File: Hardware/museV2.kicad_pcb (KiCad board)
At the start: 2 copper layers, 129 x 55.9 mm, 467 parts, among them P1 RCA_conn_x2, P10 -15V, P11 ~4, P18 RX7, P19 3.3V, P20 TX6, P21 1.8V, P22 PSU_CTL, P23 GND, P3 3.5mm_conn_tip_switch, P31 P1, P32 L1.8_1, P33 L3.3_1, P34 P2, P35 L1.8_2, P36 L3.3_2, P37 P3, P38 L1.8_3, P39 L3.3_3, P4 3.5mm_conn_tip_switch, P40 P4, P41 L1.8_4, P42 L3.3_4, P43 +5V, P5 CONN_01X06, P6 CONN_02X14, P7 ~2, P8 +15V, P9 ~3, Q1 PMOS, Q2 BSS138, SW1 PWR_BTN, SW2 PAIR_BTN, U1 TPS65130, U10 PCM1863, U11 PCM1796, U12 NE5534, U13 NE5534, U14 NE5534, U15 NE5534, U16 NE5534, U17 NE5534, U18 EdisonConnector, U19 GTL2010, U2 LP38692, U20 GTL2010, U21 GTL2010, U22 PCA9685BS, U3 PLR135/T10, U4 POM-3535L-3-R, U5 POM-3535L-3-R, U6 PLT133/T10W, U7 POM-3535L-3-R, U8 POM-3535L-3-R, U9 PCM9211, X1 24.576 MHz

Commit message: Updated text
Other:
- board text added: "Lead Hardware Designer: Jason Merlo Lead Software Designer: Steven Ploog"
- board text added: "muse v2.0.0"
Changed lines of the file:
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@@
     (links 893)
     (no_connects 152)
-    (area 103.324999 91.525 235.575001 156.088095)
+    (area 106.424999 95.424999 235.575001 151.475001)
     (thickness 1.6)
-    (drawings 4)
+    (drawings 6)
     (tracks 3081)
     (zones 0)
@@
   (page A4)
   (layers
-    (0 F.Cu signal)
-    (31 B.Cu signal)
+    (0 F.Cu signal hide)
+    (31 B.Cu signal hide)
     (32 B.Adhes user)
-    (33 F.Adhes user)
+    (33 F.Adhes user hide)
     (34 B.Paste user)
-    (35 F.Paste user)
+    (35 F.Paste user hide)
     (36 B.SilkS user)
-    (37 F.SilkS user)
+    (37 F.SilkS user hide)
     (38 B.Mask user)
-    (39 F.Mask user)
+    (39 F.Mask user hide)
     (40 Dwgs.User user)
     (41 Cmts.User user)
@@
     (45 Margin user)
     (46 B.CrtYd user)
-    (47 F.CrtYd user)
+    (47 F.CrtYd user hide)
     (48 B.Fab user hide)
     (49 F.Fab user hide)
@@
     (pad_to_mask_clearance 0.2)
     (aux_axis_origin 0 0)
-    (visible_elements FFFFFF7F)
+    (visible_elements FFFFBD7F)
     (pcbplotparams
       (layerselection 0x00030_80000001)
@@
   (module muse-v2-lib:Intel_Edison (layer F.Cu)
     (at 209.35 118.96 180)
-    (fp_text reference U18 (at 1.4 -29.1 360) (layer F.SilkS)
+    (fp_text reference U18 (at 1.4 -29.1 180) (layer F.SilkS) hide
       (effects (font (size 1 1) (thickness 0.15)))
     )
@@
     (tags "DO-214AB diode")
     (attr smd)
-    (fp_text reference D1 (at -4.117826 1.966368 180) (layer F.SilkS)
+    (fp_text reference D1 (at -4.117826 1.966368) (layer F.SilkS) hide
       (effects (font (size 1 1) (thickness 0.15)))
     )
@@
     (tags "DO-214AB diode")
     (attr smd)
-    (fp_text reference D2 (at -3.584 1.8 180) (layer F.SilkS)
+    (fp_text reference D2 (at -3.584 1.8 180) (layer F.SilkS) hide
       (effects (font (size 1 1) (thickness 0.15)))
     )
@@
   (module muse-v2-lib:7.3mm-Inductor (layer F.Cu)
     (at 162.717826 118.45 180)
-    (fp_text reference L1 (at 5 0 270) (layer F.SilkS)
+    (fp_text reference L1 (at 5 0 270) (layer F.SilkS) hide
       (effects (font (size 1 1) (thickness 0.15)))
     )
@@
   (module muse-v2-lib:7.3mm-Inductor (layer F.Cu)
     (at 176.717826 102.783632 90)
-    (fp_text reference L2 (at 4.8 0 180) (layer F.SilkS)
+    (fp_text reference L2 (at 4.8 0 180) (layer F.SilkS) hide
       (effects (font (size 1 1) (thickness 0.15)))
     )
@@
     (descr "Through hole pin header")
     (tags "pin header")
-    (fp_text reference P6 (at -2.35 -0.01 360) (layer F.SilkS)
+    (fp_text reference P6 (at -2.35 -0.01 360) (layer F.SilkS) hide
       (effects (font (size 1 1) (thickness 0.15)))
     )
@@
     (tags "resistor 0402")
     (attr smd)
-    (fp_text reference R45 (at 0 1.8 180) (layer B.SilkS)
+    (fp_text reference R45 (at 0 1.8 180) (layer B.SilkS) hide
       (effects (font (size 1 1) (thickness 0.15)) (justify mirror))
     )
@@
     (tags "resistor 0402")
     (attr smd)
-    (fp_text reference R47 (at 0 1.8 270) (layer B.SilkS)
+    (fp_text reference R47 (at 0 1.8 270) (layer B.SilkS) hide
       (effects (font (size 1 1) (thickness 0.15)) (justify mirror))
     )
@@
     (tags "resistor 0402")
     (attr smd)
-    (fp_text reference R49 (at 0 1.8 270) (layer B.SilkS)
+    (fp_text reference R49 (at 0 1.8 360) (layer B.SilkS) hide
       (effects (font (size 1 1) (thickness 0.15)) (justify mirror))
     )
@@
     (tags "resistor 0402")
     (attr smd)
-    (fp_text reference R51 (at 0 1.8 180) (layer B.SilkS)
+    (fp_text reference R51 (at 0 1.8 180) (layer B.SilkS) hide
       (effects (font (size 1 1) (thickness 0.15)) (justify mirror))
     )
@@
     (tags "resistor 0402")
     (attr smd)
-    (fp_text reference R53 (at 0 1.8 180) (layer B.SilkS)
+    (fp_text reference R53 (at 0 1.8 180) (layer B.SilkS) hide
       (effects (font (size 1 1) (thickness 0.15)) (justify mirror))
     )
@@
     (tags "resistor 0402")
     (attr smd)
-    (fp_text reference R54 (at 0 1.8 180) (layer B.SilkS)
+    (fp_text reference R54 (at 0 1.8 180) (layer B.SilkS) hide
       (effects (font (size 1 1) (thickness 0.15)) (justify mirror))
     )
@@
     (tags "SSOP 0.65")
     (attr smd)
-    (fp_text reference U19 (at 0 -5.25 180) (layer F.SilkS)
+    (fp_text reference U19 (at 0 -5.25 180) (layer F.SilkS) hide
       (effects (font (size 1 1) (thickness 0.15)))
     )
@@
     (tags "SSOP 0.65")
     (attr smd)
-    (fp_text reference U20 (at 0 -5.25) (layer F.SilkS)
+    (fp_text reference U20 (at 0 -5.25) (layer F.SilkS) hide
       (effects (font (size 1 1) (thickness 0.15)))
     )
@@
     (tags "SSOP 0.65")
     (attr smd)
-    (fp_text reference U21 (at 0 -5.25) (layer F.SilkS)
+    (fp_text reference U21 (at 0 -5.25) (layer F.SilkS) hide
       (effects (font (size 1 1) (thickness 0.15)))
     )
@@
     (tags "QFP 0.5")
     (attr smd)
-    (fp_text reference U9 (at -4.25 -4.45) (layer F.SilkS)
+    (fp_text reference U9 (at -4.25 -4.45) (layer F.SilkS) hide
       (effects (font (size 1 1) (thickness 0.15)))
     )
@@
   (module muse-v2-lib:5x3.2mm_crystal (layer F.Cu)
     (at 180.15 118.25 315)
-    (fp_text reference X1 (at -0.883883 -3.075914 315) (layer F.SilkS)
+    (fp_text reference X1 (at -0.883883 -3.075914 315) (layer F.SilkS) hide
       (effects (font (size 1 1) (thickness 0.15)))
     )
@@
     (tags "QFN 0.65")
     (attr smd)
-    (fp_text reference U22 (at -3.068321 -3.869561 315) (layer F.SilkS)
+    (fp_text reference U22 (at -3.068321 -3.869561 315) (layer F.SilkS) hide
       (effects (font (size 1 1) (thickness 0.15)))
     )
@@
     (descr "SMT capacitor, aluminium electrolytic, 4x5.3")
     (attr smd)
-    (fp_text reference C15 (at 0 -3.5433 90) (layer B.SilkS)
+    (fp_text reference C15 (at 0 -3.5433 90) (layer B.SilkS) hide
       (effects (font (size 1 1) (thickness 0.15)) (justify mirror))
     )
@@
     (descr "SMT capacitor, aluminium electrolytic, 4x5.3")
     (attr smd)
-    (fp_text reference C17 (at 0 -3.5433 180) (layer B.SilkS)
+    (fp_text reference C17 (at 0 -3.5433 180) (layer B.SilkS) hide
       (effects (font (size 1 1) (thickness 0.15)) (justify mirror))
     )
@@
     (descr "SMT capacitor, aluminium electrolytic, 4x5.3")
     (attr smd)
-    (fp_text reference C22 (at 0 -3.5433) (layer B.SilkS)
+    (fp_text reference C22 (at 0 -3.5433) (layer B.SilkS) hide
       (effects (font (size 1 1) (thickness 0.15)) (justify mirror))
     )
@@
     (descr "SMT capacitor, aluminium electrolytic, 4x5.3")
     (attr smd)
-    (fp_text reference C24 (at 0 3.5433) (layer F.SilkS)
+    (fp_text reference C24 (at 0 3.5433) (layer F.SilkS) hide
       (effects (font (size 1 1) (thickness 0.15)))
     )
@@
     (descr "SMT capacitor, aluminium electrolytic, 4x5.3")
     (attr smd)
-    (fp_text reference C38 (at 0 -3.5433 135) (layer B.SilkS)
+    (fp_text reference C38 (at 0 -3.5433 135) (layer B.SilkS) hide
       (effects (font (size 1 1) (thickness 0.15)) (justify mirror))
     )
@@
     (descr "SMT capacitor, aluminium electrolytic, 4x5.3")
     (attr smd)
-    (fp_text reference C82 (at 0 -3.5433 90) (layer B.SilkS)
+    (fp_text reference C82 (at 0 -3.5433 90) (layer B.SilkS) hide
       (effects (font (size 1 1) (thickness 0.15)) (justify mirror))
     )
@@
     (descr "SMT capacitor, aluminium electrolytic, 4x5.3")
     (attr smd)
-    (fp_text reference C87 (at 0 -3.5433 90) (layer B.SilkS)
+    (fp_text reference C87 (at 0 -3.5433 90) (layer B.SilkS) hide
       (effects (font (size 1 1) (thickness 0.15)) (justify mirror))
     )
@@
     (descr "SMT capacitor, aluminium electrolytic, 4x5.3")
     (attr smd)
-    (fp_text reference C91 (at 0 -3.5433 90) (layer B.SilkS)
+    (fp_text reference C91 (at 0 -3.5433 90) (layer B.SilkS) hide
       (effects (font (size 1 1) (thickness 0.15)) (justify mirror))
     )
@@
     )
   )
+  (gr_text "Lead Hardware Designer: Jason Merlo\nLead Software Designer: Steven Ploog" (at 233.25 105.15) (layer B.SilkS)
+    (effects (font (size 0.75 0.75) (thickness 0.125)) (justify left mirror))
+  )
+  (gr_text "muse v2.0.0\n" (at 233.45 102.35) (layer B.SilkS)
+    (effects (font (size 2 2) (thickness 0.3)) (justify left mirror))
+  )
   (gr_line (start 106.5 151.4) (end 235.5 151.4) (layer Edge.Cuts) (width 0.15))

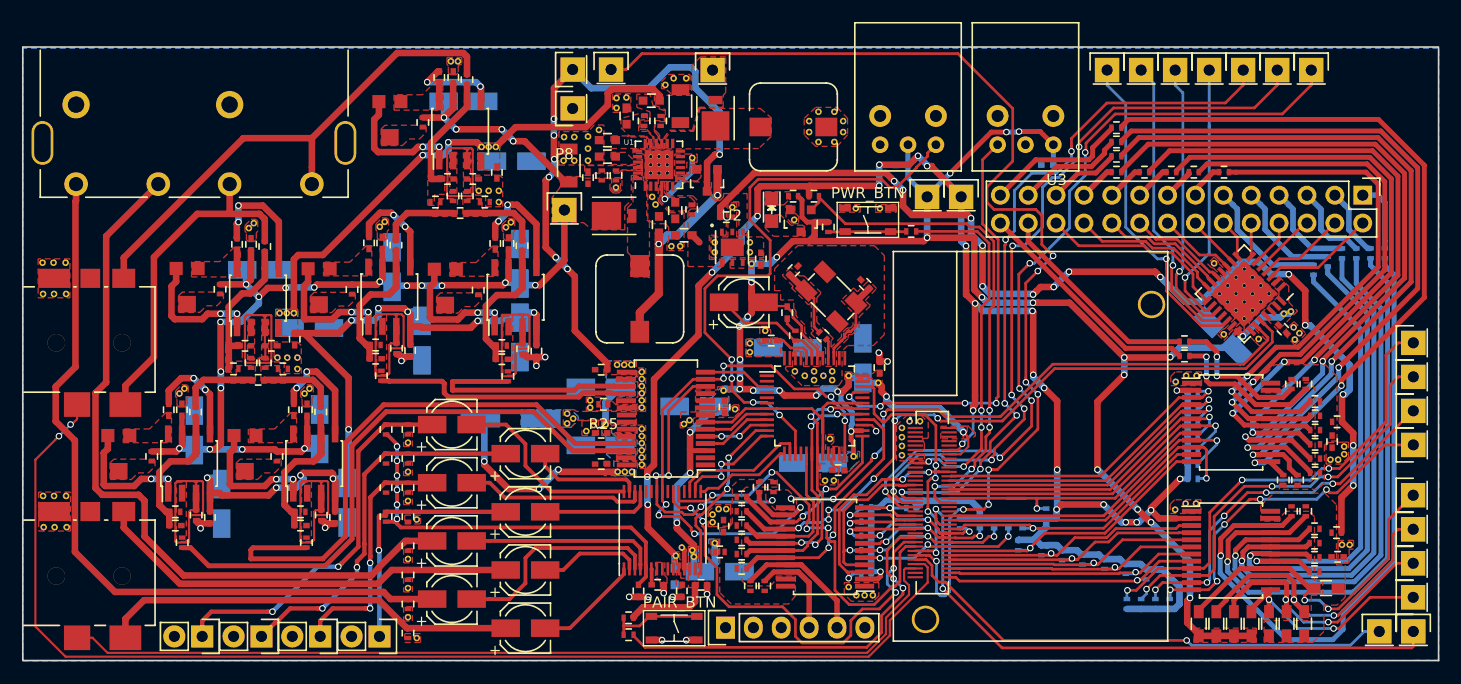
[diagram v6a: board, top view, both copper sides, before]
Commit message: Mounting holes added
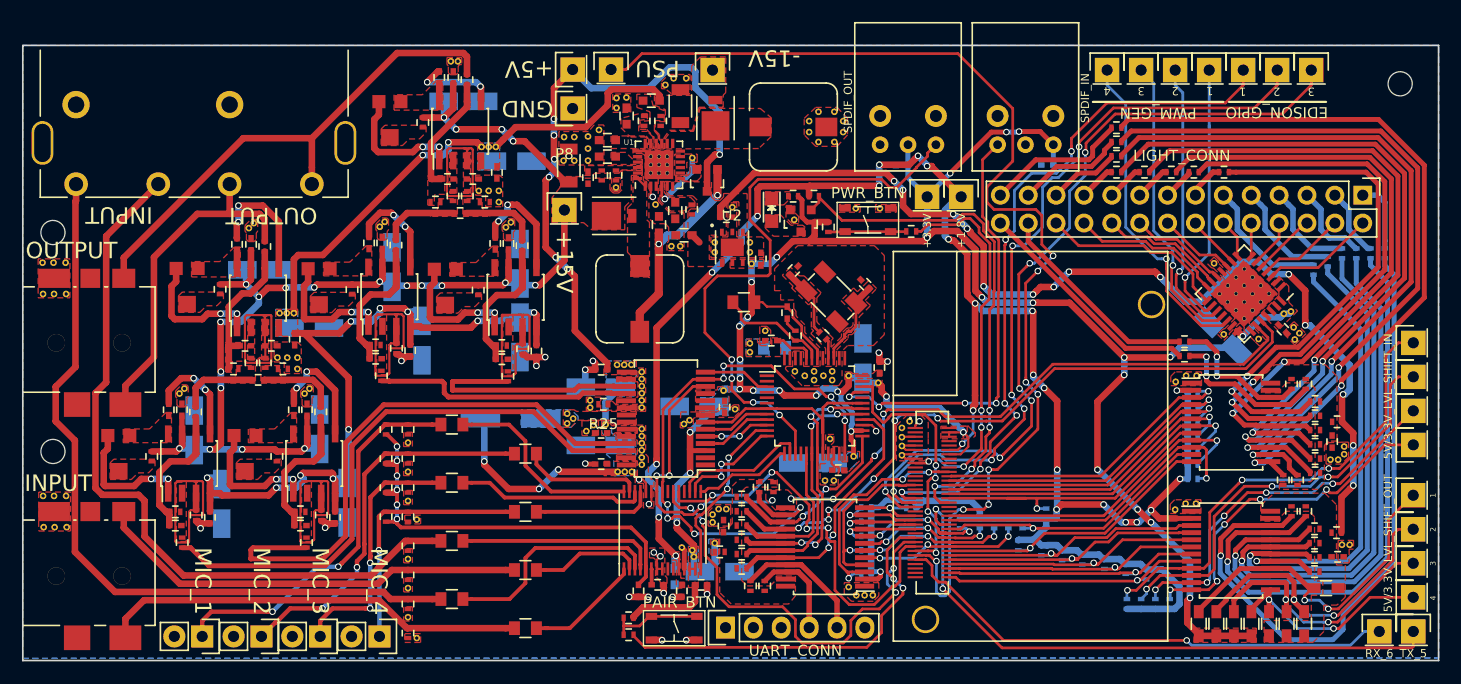
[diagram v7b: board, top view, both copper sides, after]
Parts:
- removed the REF** at (188.2, 129.6)
- removed the REF** at (163.8, 109.2)
- removed the REF** at (166.0, 141.8)
- added REF**: MountingHole_2.2mm_M2, Mounting_Holes:MountingHole_2.2mm_M2, F.Cu at (232.0, 98.8)
- added REF**: MountingHole_2.2mm_M2, Mounting_Holes:MountingHole_2.2mm_M2, F.Cu at (109.2, 132.3)
- added REF**: MountingHole_2.2mm_M2, Mounting_Holes:MountingHole_2.2mm_M2, F.Cu at (109.2, 112.4)
- C22, C24, C26, C27, C28, C29, C30, C31, C32, C33: footprint Capacitors_SMD:c_elec_4x5.3 -> Capacitors_SMD:C_0805
- P11: value ~4 -> ~3
- P18: value RX7 -> RX6
- P20: value TX6 -> TX5
- P7: value ~2 -> ~1
- P9: value ~3 -> ~2
- moved C22 1.20 mm to (175.0, 122.9)
- turned C24 to 180 degrees
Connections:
- C24 pad 1: Net-(C24-Pad1) -> +3.3VSB
- C24 pad 2: +3.3VSB -> Net-(C24-Pad2)
- R12 pad 1: Net-(C24-Pad1) -> Net-(C24-Pad2)
- U18 pad 63: 3.5_OUT_SEN -> Net-(U18-Pad63)
- U18 pad 65: 3.5_IN_SEN -> Net-(U18-Pad65)
- U9 pad 43: Net-(C24-Pad1) -> Net-(C24-Pad2)
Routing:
- net 3.5_OUT_SEN: track 110.5 -> 0.00 mm, vias 2 -> 0
- net 3.5_IN_SEN: track 83.0 -> 0.00 mm
- net GND: track 21.4 -> 40.8 mm, vias 15 -> 24
- net Net-(C24-Pad1): track 10.4 -> 0.00 mm
- net Net-(C24-Pad2): track 0.00 -> 10.2 mm
- net +3.3VSB: track 217.6 -> 220.6 mm
- net +1.8VSB: track 199.5 -> 202.3 mm, vias 24 -> 25
- net Net-(C34-Pad1): track 39.0 -> 41.2 mm
- net EDISON_PWR_BTN: track 33.2 -> 34.6 mm
- net Net-(C29-Pad2): track 9.69 -> 10.7 mm
- net Net-(D1-Pad2): track 0.00 -> 0.99 mm
- net Net-(C30-Pad2): track 17.6 -> 18.5 mm
- net EDISON_RST_OUT: track 47.4 -> 48.3 mm
- net Net-(C32-Pad2): track 16.4 -> 17.2 mm
- net Net-(C27-Pad2): track 19.7 -> 20.5 mm
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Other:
- board size 129 x 55.9 mm -> 129 x 56.1 mm
- rule trace_min: 0.2 -> 0.13
- rule via_min_size: 0.4 -> 0.305
- board text added: "+1.8V"
- board text added: "+15V"
- board text added: "+3.3V"
- board text added: "+5V"
- board text added: "-15V"
- board text added: "1"
- board text added: "2"
- board text added: "3"
- board text added: "4"
- board text added: "5V/3.3V_LVL_SHIFT_IN"
- board text added: "5V/3.3V_LVL_SHIFT_OUT"
- board text added: "EDISON_GPIO"
- board text added: "GND"
- board text added: "INPUT"
- board text added: "LIGHT_CONN"
- board text added: "MIC_1"
- board text added: "MIC_2"
- board text added: "MIC_3"
- board text added: "MIC_4"
- board text added: "OUTPUT"
- board text added: "PSU"
- board text added: "PWM_GEN"
- board text added: "RX_6"
- board text added: "SPDIF_IN"
- board text added: "SPDIF_OUT"
- board text added: "TX_5"
- board text added: "UART_CONN"
